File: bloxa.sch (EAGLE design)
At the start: 87 parts, among them CON1 PINHEAD_1X02-2.54, CON7 CON-4P-JST_GH-RA, CON8 CON-4P-JST_GH-RA, IC1 TPD3S014DBVR-SOT23-6, IC2 TJA1051(X)/3-SO8, IC6 MCP9700, Q13 BUK9K6R2-40E,115, Q14 BUK9K6R2-40E,115, Q15 BUK9K6R2-40E,115

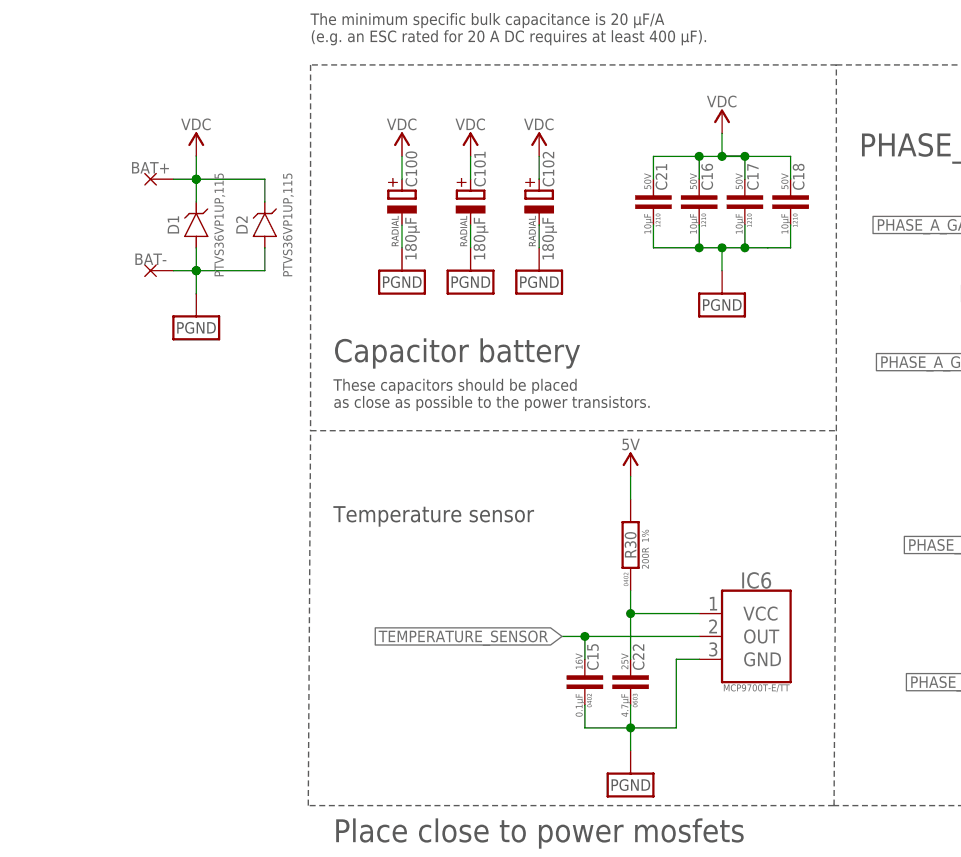
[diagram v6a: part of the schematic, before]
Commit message: all components moved to top side
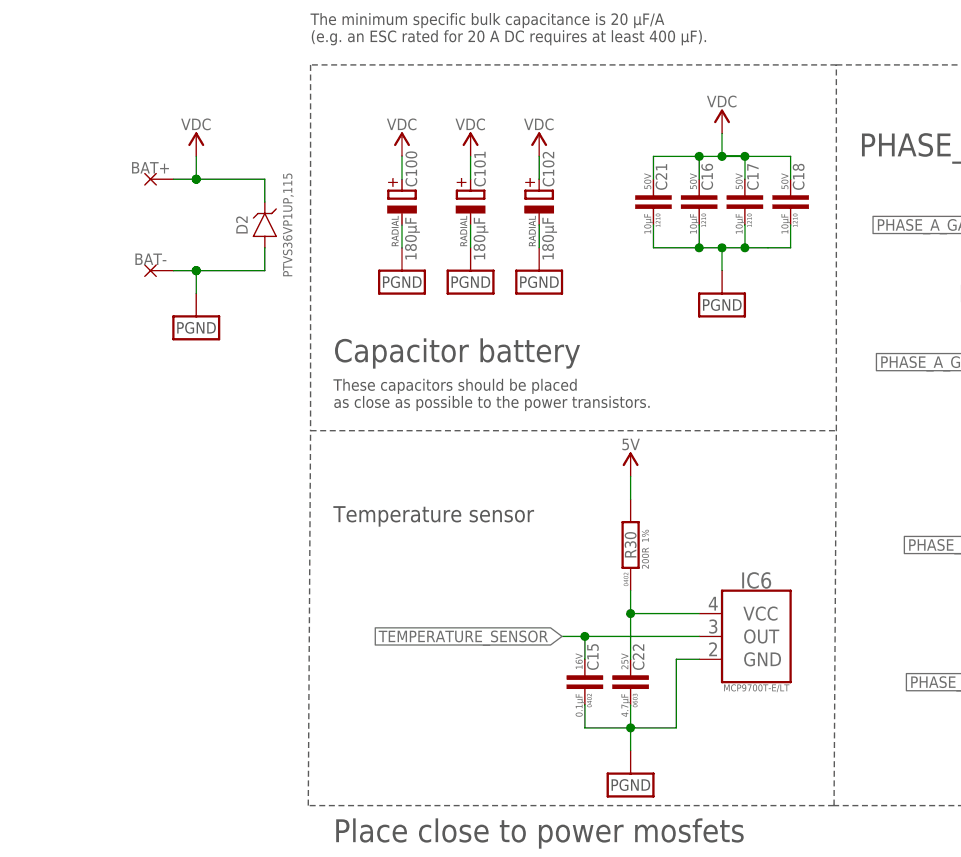
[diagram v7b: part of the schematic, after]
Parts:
- removed D1: PTVS36VP1UP,115-36V-SOD128, TVS_diodes:PTVS36VP1UP,115-36V-SOD128
- IC6: value MCP9700 -> MCP9700-SC70-5; device myxa_masterlib:MCP9700 -> misc:MCP9700-SC70-5
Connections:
- net PGND: no longer D1.A
- net VDC: no longer D1.C
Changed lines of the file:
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@@
 <variantdefs>
 <variantdef name="Basic"/>
-<variantdef name="nocaps"/>
+<variantdef name="nocaps" current="yes"/>
 </variantdefs>
 <classes>
@@
 </part>
 <part name="R26" library="SHUNT_RESISTORS" library_urn="urn:adsk.eagle:library:2644450" deviceset="CURRENT_SHUNT_KELVIN" device="-2512-KELVIN" package3d_urn="urn:adsk.eagle:package:3560627/3" technology="-0.003R" value="3 mOhms"/>
-<part name="IC6" library="myxa_masterlib" library_urn="urn:adsk.eagle:library:1040030" deviceset="MCP9700" device="" package3d_urn="urn:adsk.eagle:package:1040193/2"/>
+<part name="IC6" library="misc" library_urn="urn:adsk.eagle:library:5347860" deviceset="MCP9700" device="-SC70-5" package3d_urn="urn:adsk.eagle:package:7365869/3"/>
 <part name="R30" library="R_digikey" library_urn="urn:adsk.eagle:library:2539499" deviceset="200R" device="-0402" package3d_urn="urn:adsk.eagle:package:2539512/2" technology="-1%" value="200R"/>
 <part name="C15" library="C_digikey" library_urn="urn:adsk.eagle:library:2539367" deviceset="0.1µF" device="-0402" package3d_urn="urn:adsk.eagle:package:2539379/2" technology="-16V_10%_X7R" value="0.1µF"/>
@@
 <part name="R36" library="R_digikey" library_urn="urn:adsk.eagle:library:2539499" deviceset="4R3" device="-0402" package3d_urn="urn:adsk.eagle:package:2539512/2" technology="-5%" value="4R3"/>
 <part name="R37" library="R_digikey" library_urn="urn:adsk.eagle:library:2539499" deviceset="4R3" device="-0402" package3d_urn="urn:adsk.eagle:package:2539512/2" technology="-5%" value="4R3"/>
-<part name="S2" library="misc" library_urn="urn:adsk.eagle:library:5347860" deviceset="SENSE" device="">
+<part name="S2" library="misc" library_urn="urn:adsk.eagle:library:5347860" deviceset="SENSE" device="" package3d_urn="urn:adsk.eagle:package:7365871/1">
 <variant name="Basic" populate="no"/>
 </part>
@@
 </part>
 <part name="GND10" library="supply_symbols" library_urn="urn:adsk.eagle:library:5017758" deviceset="PGND" device="" value="PGND"/>
-<part name="D1" library="TVS_diodes" library_urn="urn:adsk.eagle:library:3333632" deviceset="PTVS36VP1UP,115" device="-SOD128" package3d_urn="urn:adsk.eagle:package:6533206/2" technology="-36V"/>
 <part name="D2" library="TVS_diodes" library_urn="urn:adsk.eagle:library:3333632" deviceset="PTVS36VP1UP,115" device="-SOD128" package3d_urn="urn:adsk.eagle:package:6533206/2" technology="-36V"/>
 <part name="C100" library="rc" library_urn="urn:adsk.eagle:library:2539423" deviceset="CPOL" device="-RADIAL_SIDE-8X21.5" package3d_urn="urn:adsk.eagle:package:7189333/2" value="180µF">
@@
 <attribute name="VALUE" x="119.38" y="217.17" size="1.27" layer="97" font="vector" ratio="15" align="center"/>
 </instance>
-<instance part="D1" gate="G$1" x="119.38" y="228.6" smashed="yes" rot="R90">
-<attribute name="NAME" x="116.84" y="228.6" size="1.27" layer="95" font="vector" ratio="15" rot="R90" align="center"/>
-<attribute name="MANF#" x="121.92" y="228.6" size="1.016" layer="95" font="vector" ratio="15" rot="R90" align="center"/>
-</instance>
 <instance part="D2" gate="G$1" x="127" y="228.6" smashed="yes" rot="R90">
 <attribute name="NAME" x="124.46" y="228.6" size="1.27" layer="95" font="vector" ratio="15" rot="R90" align="center"/>
@@
 <wire x1="119.38" y1="220.98" x2="119.38" y2="223.52" width="0.1524" layer="91"/>
 <junction x="119.38" y="223.52"/>
-<pinref part="D1" gate="G$1" pin="A"/>
-<wire x1="119.38" y1="226.06" x2="119.38" y2="223.52" width="0.1524" layer="91"/>
 <junction x="119.38" y="223.52"/>
 <wire x1="119.38" y1="223.52" x2="127" y2="223.52" width="0.1524" layer="91"/>
@@
 <segment>
 <pinref part="D2" gate="G$1" pin="C"/>
-<pinref part="D1" gate="G$1" pin="C"/>
 <wire x1="116.84" y1="233.68" x2="119.38" y2="233.68" width="0.1524" layer="91"/>
 <junction x="119.38" y="233.68"/>
-<wire x1="119.38" y1="233.68" x2="119.38" y2="231.14" width="0.1524" layer="91"/>
 <junction x="119.38" y="233.68"/>
 <wire x1="119.38" y1="233.68" x2="127" y2="233.68" width="0.1524" layer="91"/>

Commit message: routing complete
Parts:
- removed C22: 4.7µF, C_digikey:4.7µF-25V_10%_X6S-0603
- removed R30: 200R, R_digikey:200R-1%-0402
- added C1: 0.1µF, C_digikey:0.1µF-16V_10%_X7R-0402
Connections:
- removed net N$1: C22.2, IC6.VCC, R30.1
- removed net N$5: CON7.4, CON8.4
- net GND: no longer C11.2, C3.2, IC2.GND
- net GNDD: now also CON7.4, CON8.4
- net PGND: now also C1.2, C11.2, C15.2, C3.2, IC2.GND; no longer C15.1, C22.1
- net TEMPERATURE_SENSOR: now also C1.1; no longer C15.2
- net VDD_5V: now also C15.1, IC6.VCC; no longer R30.2
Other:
- moved on the sheet: C11, C15, D2, IC6
